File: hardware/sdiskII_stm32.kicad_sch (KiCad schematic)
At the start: 21 parts, among them J1 Micro_SD_Card, J3 APPLE_SDISKII, U1 74LS123, U2 74LS123, U3 74LS06, U4 74LS125, U5 STM32F401CCUx, U6 74LS393, U7 74LS74, U8 74LS86

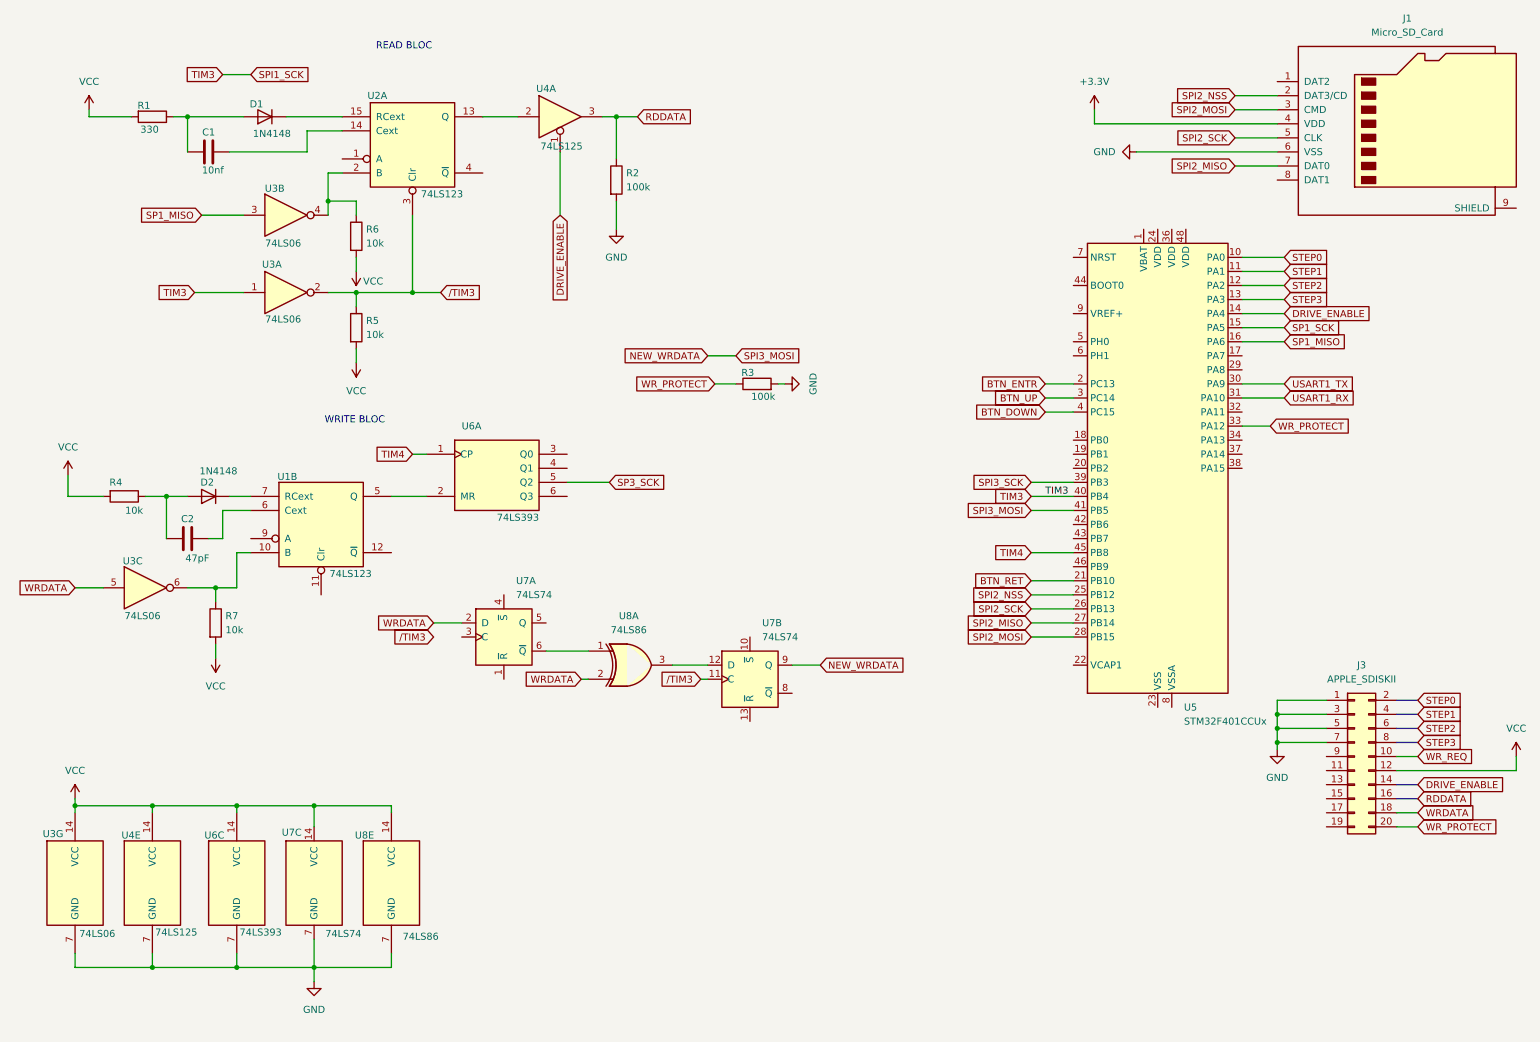
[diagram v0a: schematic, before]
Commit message: Start working on write process, WR_REQ working, complete change of PIN, SPI with variable clock ...
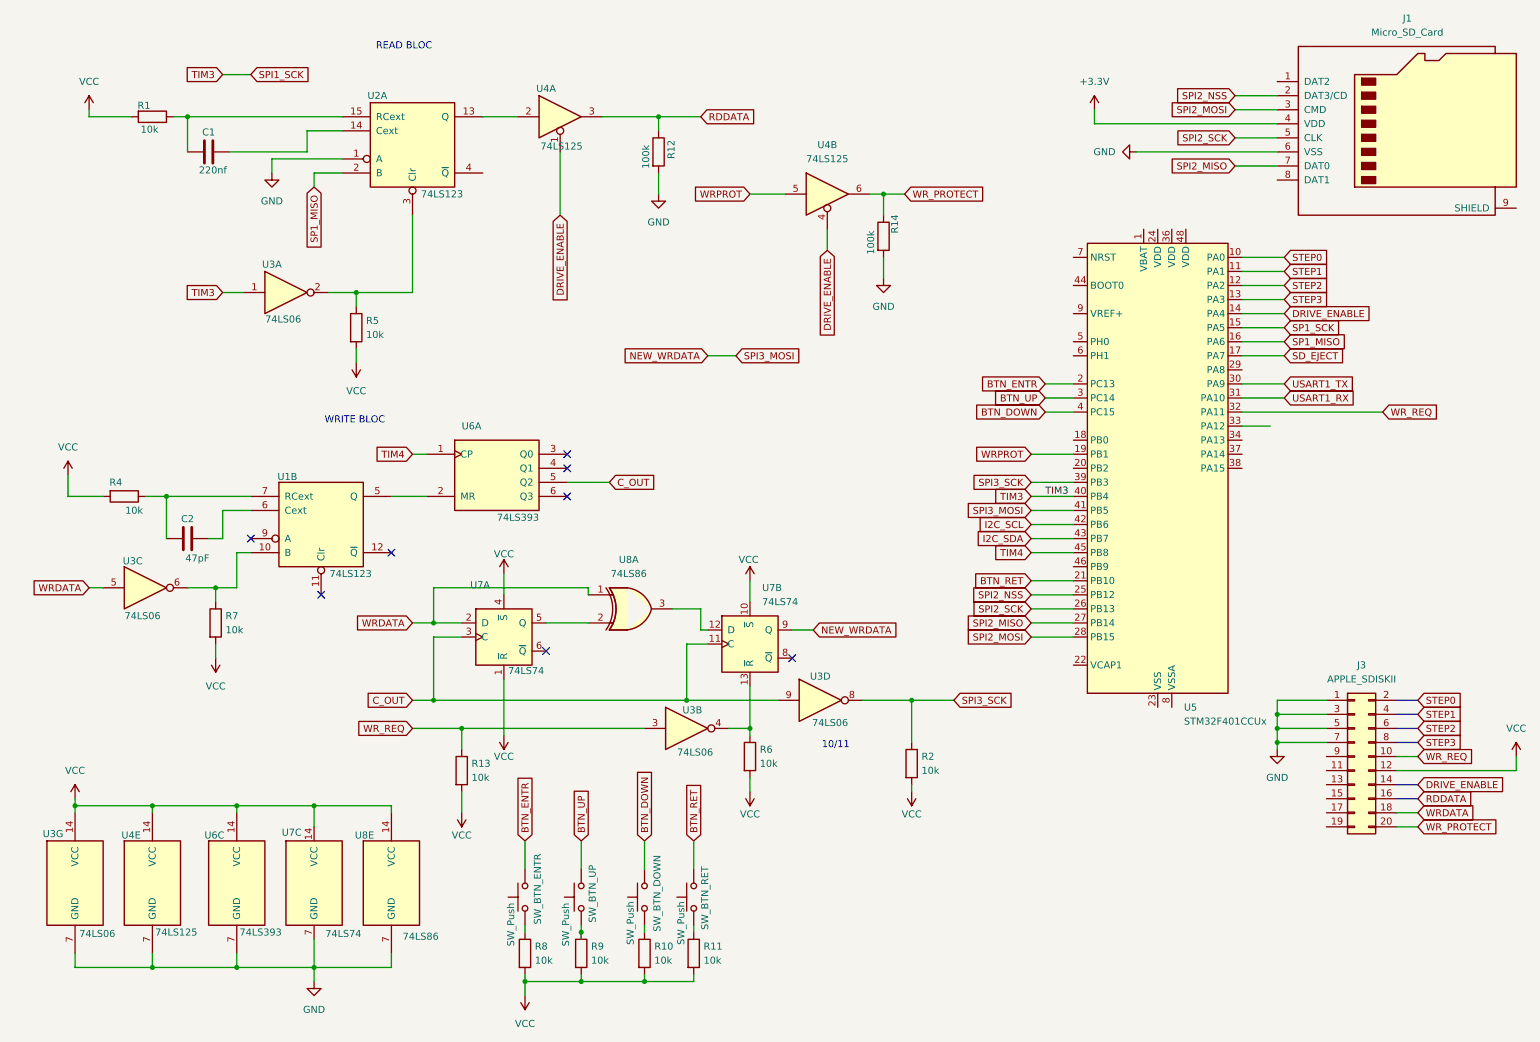
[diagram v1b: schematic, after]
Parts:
- removed D1, D2: 1N4148, symbol Device:D
- removed R3: 100k, symbol Device:R
- added R10, R11, R13, R8, R9: 10k, symbol Device:R
- added R12, R14: 100k, symbol Device:R
- added SW_BTN_DOWN, SW_BTN_ENTR, SW_BTN_RET, SW_BTN_UP: SW_Push, symbol Switch:SW_Push
- added unit 4 of U3
- added unit 2 of U4
- C1: value 10nf -> 220nf
- R1: value 330 -> 10k
- R2: value 100k -> 10k
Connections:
- net SP3_SCK is gone; now on net C_OUT: U6.5 (Q2)
- net BTN_DOWN: now also SW_BTN_DOWN.2
- net BTN_ENTR: now also SW_BTN_ENTR.2
- net BTN_RET: now also SW_BTN_RET.2
- net BTN_UP: now also SW_BTN_UP.2
- net DRIVE_ENABLE: now also U4.4
- net GND: now also U2.1 (A), R12.2, R14.2; no longer R2.2
- net RDDATA: now also R12.1; no longer R2.1
- net SP1_MISO: now also U2.2 (B); no longer U3.3
- net SPI3_SCK: now also R2.1, U3.8
- net VCC: now also R2.2, U7.1 (~{R}), U7.10 (~{S}), U7.4 (~{S}), R10.2, R11.2, R13.2, R8.2, R9.2
- net WRDATA: now also U8.1; no longer U8.2
- net WR_PROTECT: now also R14.1, U4.6; no longer U5.33 (PA12)
- net WR_REQ: now also U3.3, U5.32 (PA11), R13.1
- net SD_EJECT: now reaches U5.17 (PA7)
- net WRPROT: now reaches U5.19 (PB1)
- net WRPROT: now also U4.5
- net I2C_SCL: now reaches U5.42 (PB6)
- net I2C_SDA: now reaches U5.43 (PB7)
- net at U2.15 (RCext): now also C1.1, R1.1
- net at U1.7 (RCext): now also C2.1, R4.1
- net at R6.1, U3.4: now also U7.13 (~{R}); no longer U2.2 (B)
- net C_OUT: now reaches U7.3 (C)
- net C_OUT: now also U7.11 (C), U3.9
- net at U7.5 (Q): now also U8.2
- net at U7.6 (~{Q}): no longer U8.1
- net /TIM3: no longer names the net of R5.1, U2.3 (Clr), U3.2
- net /TIM3: no longer U7.11 (C)
- new net: R11.1, SW_BTN_RET.1
- new net: R8.1, SW_BTN_ENTR.1
- new net: R10.1, SW_BTN_DOWN.1
- new net: R9.1, SW_BTN_UP.1
- no-connect marks 0 -> 8
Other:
- note added: "10/11"
- title: (none) -> APPLE II DISK EM
- moved on the sheet: U7B, U8A

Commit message: fix writing overlap, add log lib
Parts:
- removed R2, R5, R6, R7: 10k, symbol Device:R
- removed U3: 74LS06, symbol 74xx:74LS06
- added C3, C5: 10uF, symbol Device:C_Polarized
- added U3: LM1117MP-3.3, Package_TO_SOT_SMD:SOT-223-3_TabPin2, symbol Regulator_Linear:LM1117MP-3.3
- added unit 2 of U6
- added U9: 74LS14, symbol 74xx:74LS14
- C1: value 220nf -> 220pF
- R12, R14: value 100k -> 1k
- R13: value 10k -> 1k
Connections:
- net +3.3V: now also C5.1, U3.2 (VO)
- net C_OUT: now also U6.11 (Q0), U9.9; no longer U6.5 (Q2)
- net DRIVE_ENABLE: now also U9.11; no longer U5.14 (PA4)
- net GND: now also U1.9 (A), C3.2, C5.2, U3.1 (GND), U9.7 (GND); no longer R12.2, R14.2
- net SD_EJECT: now also J1.9 (SHIELD)
- net SPI1_SCK: now also U9.1
- net SPI3_SCK: now also U9.8
- net VCC: now also R12.2, R14.1, C3.1, U3.3 (VI), U9.14 (VCC)
- net WRDATA: now also U9.5; no longer U7.2 (D), U8.1
- net WR_PROTECT: now also R14.2; no longer R14.1
- net WR_REQ: now also U9.3
- net /WRDATA: now reaches U1.10 (B)
- net /WRDATA: now also U7.2 (D), U8.1, U9.6
- net at U1.5 (Q), U6.2 (MR): now also U6.12 (MR)
- net at U1.6 (Cext): now also C2.1; no longer C2.2
- net at R4.1, U1.7 (RCext): now also C2.2; no longer C2.1
- net /WR_REQ: now reaches U7.13 (~{R})
- net /WR_REQ: now also U9.4
- net at U2.3 (Clr): now also U9.2
- net at U6.6 (Q3): now also U6.13 (CP)
- new net /DRIVE_ENABLE: U5.14 (PA4), U9.10
- no-connect marks 8 -> 11
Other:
- note added: "LS393 counting to 16"
- note added: "POWER BLOCK"
- note added: "TIM3 250KHz (255/128)"
- note added: "TIM4 8MHz (7/4)"
- note removed: "10/11"
- title: APPLE II DISK EM -> APPLE II DISK EM STM32F401
- moved on the sheet: C1, C2, J3, R1, R10, R11, R12, R13, R14, R4, R8, R9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
